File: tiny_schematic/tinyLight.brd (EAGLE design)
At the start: 52 x 33.2 mm, 38 parts, among them IC1 NCP1117, IC2 XMEGA-A4TQFP, IC3 CM1293A-02SR, J1 RASM722PX, J2 Molex, J3 PDI, Q1 BC849SMD, Q2 BC849SMD, X1 MICRO-USB

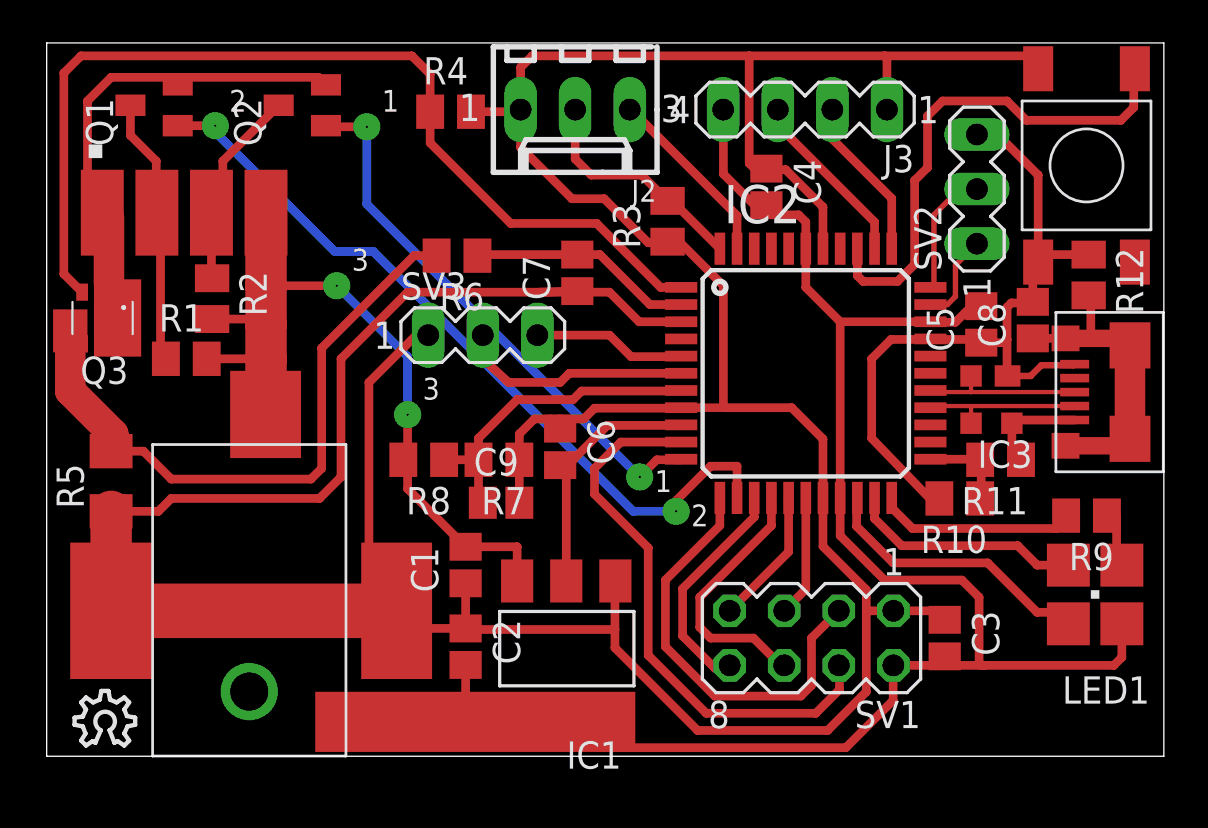
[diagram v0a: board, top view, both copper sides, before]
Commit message: BT-Module finished IR-header moved
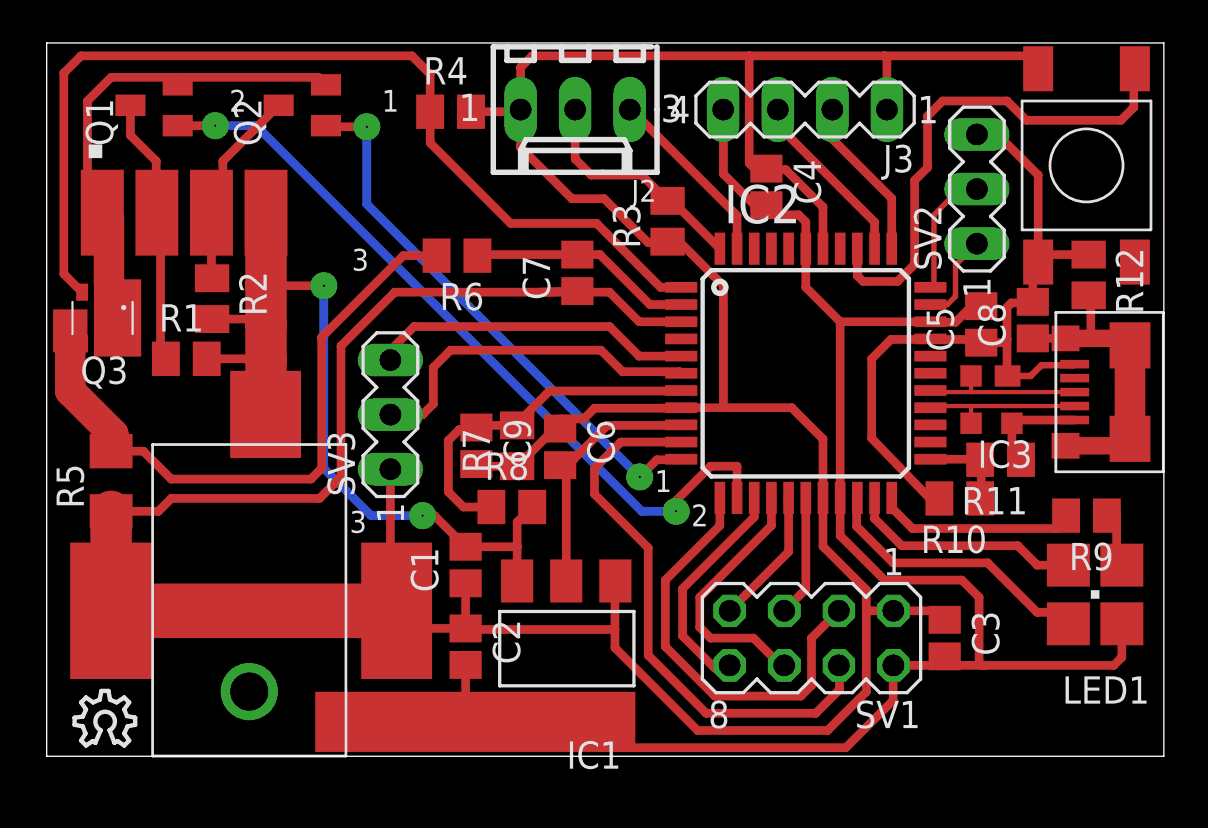
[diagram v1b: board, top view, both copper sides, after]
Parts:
- moved SV3 5.67 mm to (16.0, 15.9), turned to 90 degrees
- moved R8 4.65 mm to (21.6, 11.6), turned to 0 degrees
- moved C9 2.89 mm to (20.0, 14.4), turned to 270 degrees
- moved R7 1.07 mm to (21.9, 14.4), turned to 90 degrees
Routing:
- net GND: track 234.2 -> 225.6 mm
- net N$27: track 7.12 -> 15.0 mm
- net N$2: track 11.0 -> 16.3 mm
- net +5V: track 37.3 -> 40.6 mm
- net U_PSU: track 15.1 -> 16.5 mm

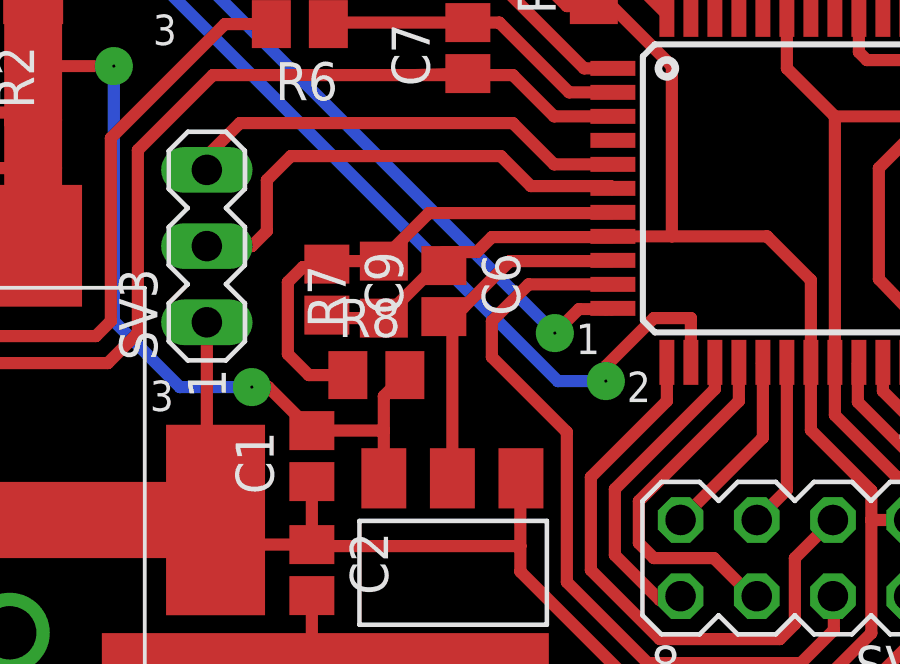
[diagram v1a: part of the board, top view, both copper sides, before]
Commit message: Improved clearance
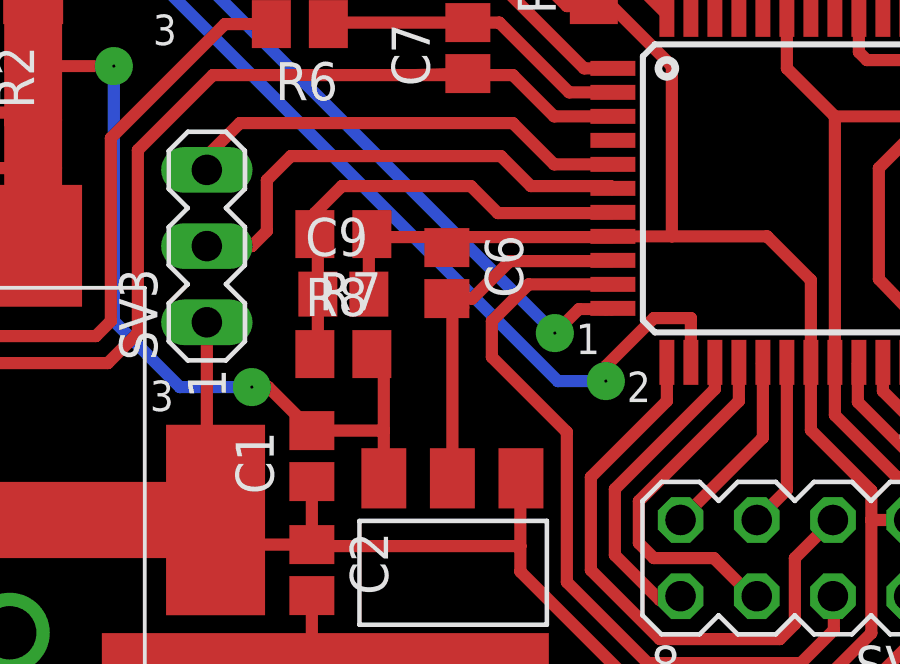
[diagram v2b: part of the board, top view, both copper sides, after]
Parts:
- moved R7 2.29 mm to (20.6, 16.3), turned to 180 degrees
- moved R8 1.30 mm to (20.6, 12.3)
- moved C6 0.61 mm to (24.0, 15.0)
- moved C9 0.57 mm to (20.6, 14.3), turned to 0 degrees
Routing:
- net U_PSU: track 16.5 -> 15.5 mm
- net +3V3: track 92.6 -> 93.4 mm
- net +5V: track 40.6 -> 41.1 mm
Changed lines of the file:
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@@
 <attribute name="OC_FARNELL" value="unknown" x="24.6" y="30.1" size="1.778" layer="27" rot="R180" display="off"/>
 </element>
-<element name="R8" library="rcl" package="M2012" value="5.6k" x="21.65" y="11.6"/>
-<element name="R7" library="rcl" package="M2012" value="1k" x="21.9" y="14.45" rot="R90"/>
+<element name="R8" library="rcl" package="M2012" value="5.6k" x="20.55" y="12.3"/>
+<element name="R7" library="rcl" package="M2012" value="1k" x="20.55" y="16.3" rot="R180"/>
 <element name="R5" library="rcl" package="M3216" value="15m" x="3" y="12.8" rot="R90"/>
 <element name="JP1" library="tinyLight" package="LED-STRIPE" value="RGB-LED-STRIPE" x="6.4" y="25.3"/>
@@
 <attribute name="OC_FARNELL" value="unknown" x="35.3" y="30.1" size="1.778" layer="27" rot="R180" display="off"/>
 </element>
-<element name="C6" library="rcl" package="C2012" value="100nF" x="23.9" y="14.4" rot="R270"/>
+<element name="C6" library="rcl" package="C2012" value="100nF" x="24" y="15" rot="R270"/>
 <element name="R10" library="rcl" package="M2012" value="1.5k" x="42.5" y="12" rot="R180"/>
 <element name="R12" library="rcl" package="M2012" value="1M" x="48.5" y="22.4" rot="R270"/>
@@
 <element name="U$9" library="ohw-logo" package="OSHW_8X100_NOTEXT" value="" x="1.3" y="0.5"/>
 <element name="S1" library="tinyLight" package="LSH_6X6" value="SPST_PB" x="48.4" y="27.5" rot="R270"/>
-<element name="C9" library="rcl" package="C2012" value="100nF" x="20" y="14.45" rot="R270"/>
+<element name="C9" library="rcl" package="C2012" value="100nF" x="20.55" y="14.3"/>
 <element name="SV1" library="con-lstb" package="MA04-2" value="" x="35.6" y="5.5" rot="R180">
 <attribute name="OC_NEWARK" value="unknown" x="35.6" y="5.5" size="1.778" layer="27" rot="R180" display="off"/>
@@
 <wire x1="48.5" y1="23.35" x2="46.05" y2="23.35" width="0.4064" layer="1"/>
 <wire x1="29.534115625" y1="16.22409375" x2="29.510021875" y2="16.2" width="0.4064" layer="1"/>
-<wire x1="29.510021875" y1="16.2" x2="25.5" y2="16.2" width="0.4064" layer="1"/>
+<wire x1="29.510021875" y1="16.2" x2="24" y2="16.2" width="0.4064" layer="1"/>
 <contactref element="R4" pad="2"/>
 <contactref element="C7" pad="1"/>
 <contactref element="S1" pad="4" route="any" routetag="2"/>
 <contactref element="S1" pad="3" route="any" routetag="2"/>
+<wire x1="24" y1="16.2" x2="21.6" y2="16.2" width="0.4064" layer="1"/>
 <wire x1="46.15" y1="23" x2="46.05" y2="23.35" width="0.4064" layer="1"/>
 <wire x1="46.15" y1="23" x2="45.95" y2="22.65" width="0.4064" layer="1"/>
@@
 <wire x1="5.8" y1="12" x2="5.2" y2="11.4" width="0.4064" layer="1"/>
 <wire x1="5.2" y1="11.4" x2="3" y2="11.4" width="0.4064" layer="1"/>
-<wire x1="25.5" y1="16.2" x2="25" y2="15.7" width="0.4064" layer="1"/>
-<wire x1="23.95" y1="15.7" x2="23.9" y2="15.25" width="0.4064" layer="1"/>
+<wire x1="23.95" y1="15.7" x2="24" y2="15.85" width="0.4064" layer="1"/>
 <wire x1="47.8481375" y1="18.2501375" x2="47.798" y2="18.2" width="0.3048" layer="1"/>
 <wire x1="47.798" y1="18.2" x2="46.3" y2="18.2" width="0.3048" layer="1"/>
@@
 <wire x1="38.15" y1="7.75" x2="38.15" y2="6.77" width="0.4064" layer="1"/>
 <wire x1="38.15" y1="6.77" x2="39.41" y2="6.77" width="0.4064" layer="1"/>
-<wire x1="25" y1="15.7" x2="23.95" y2="15.7" width="0.4064" layer="1"/>
 <contactref element="SV2" pad="3"/>
 <wire x1="19.75" y1="30" x2="21.96" y2="30" width="0.4064" layer="1"/>
@@
 <wire x1="39.3" y1="19.4" x2="41.110021875" y2="19.4" width="0.4064" layer="1"/>
 <wire x1="41.110021875" y1="19.4" x2="41.134115625" y2="19.42409375" width="0.4064" layer="1"/>
-<wire x1="23.85" y1="15.7" x2="23.9" y2="15.25" width="0.4064" layer="1"/>
+<wire x1="23.85" y1="15.7" x2="24" y2="15.85" width="0.4064" layer="1"/>
 <wire x1="15" y1="6.97" x2="15.2" y2="6.77" width="0.4064" layer="1"/>
 <wire x1="16.2" y1="21.6" x2="13.7" y2="19.1" width="0.4064" layer="1"/>
 <wire x1="16" y1="13.36" x2="16" y2="7.06" width="0.4064" layer="1"/>
 <wire x1="16" y1="7.06" x2="16.29" y2="6.77" width="0.4064" layer="1"/>
-<wire x1="20" y1="13.6" x2="20.1" y2="13.5" width="0.4064" layer="1"/>
-<wire x1="20.1" y1="13.5" x2="21.9" y2="13.5" width="0.4064" layer="1"/>
-<wire x1="21.9" y1="13.5" x2="23.65" y2="15.25" width="0.4064" layer="1"/>
-<wire x1="23.65" y1="15.25" x2="23.9" y2="15.25" width="0.4064" layer="1"/>
+<wire x1="21.5" y1="16.3" x2="21.4" y2="16.2" width="0.4064" layer="1"/>
+<wire x1="21.4" y1="16.2" x2="21.4" y2="14.3" width="0.4064" layer="1"/>
+<wire x1="21.6" y1="16.2" x2="21.5" y2="16.3" width="0.4064" layer="1"/>
+<wire x1="23.85" y1="15.7" x2="23.85" y2="16.05" width="0.4064" layer="1"/>
+<wire x1="23.85" y1="16.05" x2="24" y2="16.2" width="0.4064" layer="1"/>
 </signal>
 <signal name="USB_P">
@@
 <wire x1="41.134115625" y1="20.22409375" x2="36.934115625" y2="20.22409375" width="0.4" layer="1"/>
 <contactref element="IC2" pad="39"/>
-<wire x1="24.55" y1="13.85" x2="26.1" y2="15.4" width="0.4064" layer="1"/>
 <wire x1="26.1" y1="15.4" x2="29.510021875" y2="15.4" width="0.4064" layer="1"/>
 <wire x1="29.510021875" y1="15.4" x2="29.534115625" y2="15.42409375" width="0.4064" layer="1"/>
@@
 <wire x1="19.5" y1="1.8604" x2="24.21" y2="1.8604" width="0.4064" layer="1"/>
 <wire x1="24.55" y1="13.85" x2="23.5" y2="13.85" width="0.4064" layer="1"/>
-<wire x1="24.55" y1="13.85" x2="24.1846" y2="13.4846" width="0.4064" layer="1"/>
-<wire x1="24.1846" y1="13.4846" x2="24.1846" y2="8.1596" width="0.4064" layer="1"/>
+<wire x1="24.1846" y1="14.15" x2="24.1846" y2="8.1596" width="0.4064" layer="1"/>
 <wire x1="24.21" y1="1.8604" x2="25.7704" y2="0.4" width="0.4064" layer="1"/>
 <wire x1="25.7704" y1="0.4" x2="37.2" y2="0.4" width="0.4064" layer="1"/>
@@
 <wire x1="49.67" y1="4.23" x2="50.045" y2="4.605" width="0.4064" layer="1"/>
 <wire x1="50.045" y1="4.605" x2="50.045" y2="6.165" width="0.4064" layer="1"/>
-<wire x1="23.5" y1="13.85" x2="23.9" y2="13.55" width="0.4064" layer="1"/>
+<wire x1="23.5" y1="13.85" x2="24" y2="14.15" width="0.4064" layer="1"/>
+<wire x1="26.1" y1="15.4" x2="24.85" y2="14.15" width="0.4064" layer="1"/>
+<wire x1="24.85" y1="14.15" x2="24" y2="14.15" width="0.4064" layer="1"/>
+<wire x1="24.1846" y1="14.15" x2="24" y2="14.15" width="0.4064" layer="1"/>
 </signal>
 <signal name="+5V">
@@
 <wire x1="7.7" y1="20.35" x2="10.21" y2="20.35" width="0.4064" layer="1"/>
 <wire x1="10.21" y1="20.35" x2="10.21" y2="20.1" width="0.4064" layer="1"/>
-<wire x1="22.6" y1="11.6" x2="21.8986" y2="10.8986" width="0.4064" layer="1"/>
-<wire x1="21.8986" y1="10.8986" x2="21.8986" y2="9.75" width="0.4064" layer="1"/>
+<wire x1="21.5" y1="12.3" x2="21.8986" y2="11.6986" width="0.4064" layer="1"/>
+<wire x1="21.8986" y1="11.6986" x2="21.8986" y2="9.75" width="0.4064" layer="1"/>
 <via x="17.5" y="11.2" extent="1-16" drill="0.1" diameter="1.27" shape="octagon"/>
 <wire x1="17.5" y1="11.2" x2="18.05" y2="11.2" width="0.4064" layer="1"/>
@@
 <contactref element="C9" pad="1"/>
 <wire x1="29.510021875" y1="17" x2="29.534115625" y2="17.02409375" width="0.4064" layer="1"/>
-<wire x1="29.510021875" y1="17" x2="23.4" y2="17" width="0.4064" layer="1"/>
-<wire x1="20" y1="15.3" x2="20.1" y2="15.4" width="0.4064" layer="1"/>
-<wire x1="20.1" y1="15.4" x2="21.9" y2="15.4" width="0.4064" layer="1"/>
-<wire x1="23.4" y1="17" x2="21.9" y2="15.5" width="0.4064" layer="1"/>
-<wire x1="21.9" y1="15.5" x2="21.9" y2="15.4" width="0.4064" layer="1"/>
-<wire x1="20" y1="15.3" x2="19.9" y2="15.2" width="0.4064" layer="1"/>
-<wire x1="19.9" y1="15.2" x2="19.2" y2="15.2" width="0.4064" layer="1"/>
-<wire x1="19.2" y1="15.2" x2="18.7" y2="14.7" width="0.4064" layer="1"/>
-<wire x1="18.7" y1="14.7" x2="18.7" y2="12.3" width="0.4064" layer="1"/>
-<wire x1="18.7" y1="12.3" x2="19.4" y2="11.6" width="0.4064" layer="1"/>
-<wire x1="19.4" y1="11.6" x2="20.7" y2="11.6" width="0.4064" layer="1"/>
+<wire x1="19.6" y1="12.3" x2="19.7" y2="12.3" width="0.4064" layer="1"/>
+<wire x1="19.7" y1="12.3" x2="19.7" y2="14.3" width="0.4064" layer="1"/>
+<wire x1="19.7" y1="14.3" x2="19.7" y2="16.2" width="0.4064" layer="1"/>
+<wire x1="19.7" y1="16.2" x2="19.6" y2="16.3" width="0.4064" layer="1"/>
+<wire x1="29.510021875" y1="17" x2="25.7" y2="17" width="0.4064" layer="1"/>
+<wire x1="25.7" y1="17" x2="24.8" y2="17.9" width="0.4064" layer="1"/>
+<wire x1="24.8" y1="17.9" x2="20.5" y2="17.9" width="0.4064" layer="1"/>
+<wire x1="20.5" y1="17.9" x2="19.6" y2="17" width="0.4064" layer="1"/>
+<wire x1="19.6" y1="17" x2="19.6" y2="16.3" width="0.4064" layer="1"/>
 </signal>
 <signal name="I_LED">

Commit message: bootloader ported to new hardware
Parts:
- C2: value 110µF -> 10µF
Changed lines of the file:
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@@
 <element name="R11" library="rcl" package="M2012" value="1k" x="44.4" y="13.8" rot="R180"/>
 <element name="C1" library="rcl" package="C2012" value="10µF" x="19.5" y="8.9" rot="R90"/>
-<element name="C2" library="rcl" package="C2012" value="110µF" x="19.5" y="5.1" rot="R270"/>
+<element name="C2" library="rcl" package="C2012" value="10µF" x="19.5" y="5.1" rot="R270"/>
 <element name="R9" library="rcl" package="M2012" value="150" x="48.4" y="11.2" rot="R180"/>
 <element name="C3" library="rcl" package="C2012" value="100nF" x="41.8" y="5.5" rot="R270"/>
